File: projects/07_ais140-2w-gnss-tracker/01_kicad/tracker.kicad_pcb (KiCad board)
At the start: 4 copper layers, 60 x 45 mm, 174 parts, among them J1 VEHICLE 2x4, J2 BATTERY 18650, J3 USB-C, J4 DEBUG TC2050, J5 NANO-SIM, J6 LTE ANT, J7 GNSS ANT, Q1 BUK7M12-60EX, Q2 2N7002, Q3 MMBT3904, Q4 BUK9M53-60EX, SW1 RESET, SW2 BOOT, U1 LM74700-Q1, U10 W25Q128JV, U11 SIM7080G, U12 TXS0108E, U13 ESDA6V1-5SC6, U14 NEO-F10N, U15 IIM-42652, U16 RV-3028-C7, U2 LM5164-Q1, U3 BQ24074, U4 LC709203F, U5 TLV75733P, U6 TPS22917, U7 TPS22917, U8 ESP32-S3-WROOM-1-N8R2, U9 USBLC6-2SC6

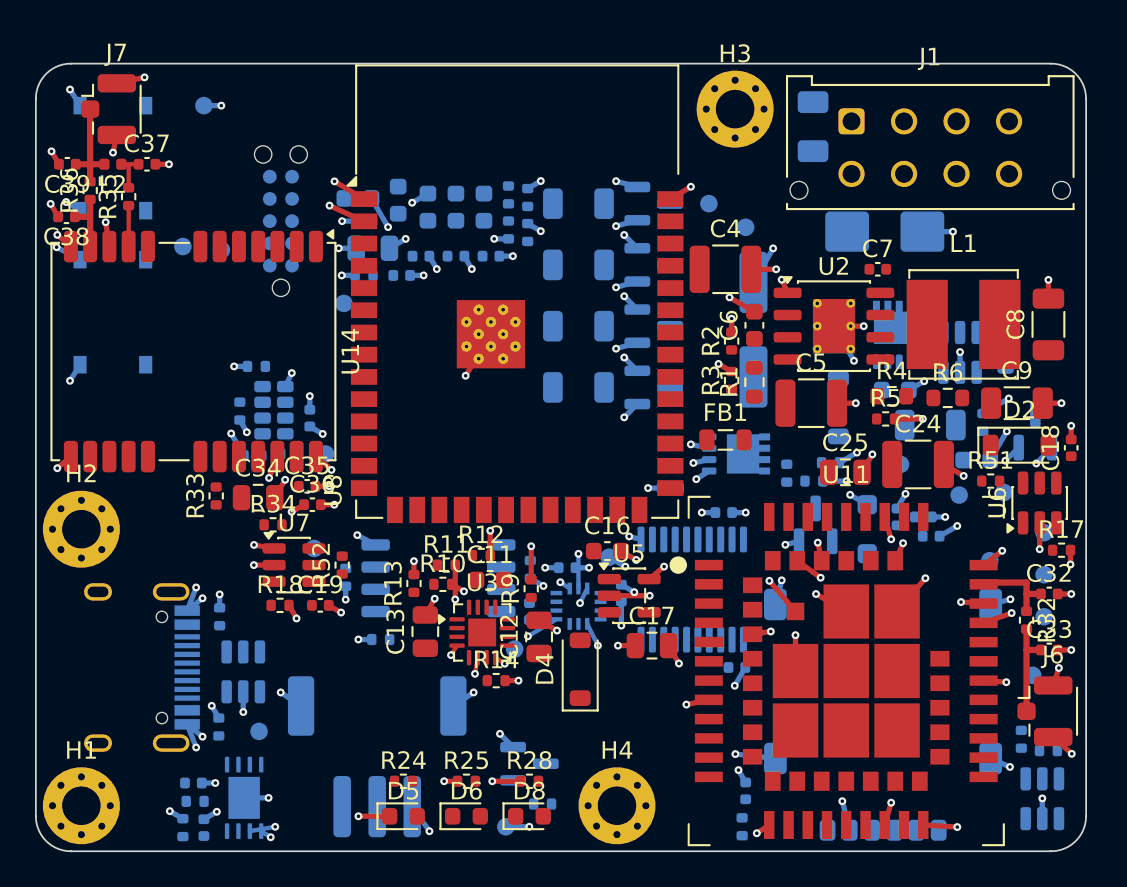
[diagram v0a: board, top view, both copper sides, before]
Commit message: Project 07: routed 4-layer PCB, fab outputs and 3D for the AIS-140 tracker
- 60x45 mm 4-layer board, double-sided assembly: KiCad DRC 0 errors / 0 unconnected,
  schematic parity clean, ERC clean
- Flow: anchors + greedy placer, GND/+3V3 fan-out, Freerouting 1.9, grid A* finisher
  with rip-up, RF via fences, edge/area stitching, island vias
- Gerbers + drill (zip), JLC BOM/CPL, engineering BOM, assembly PDFs, STEP + renders
  (envelope models for parts without a KiCad 3D model)
- Programming/JTAG via pogo test pads TP21-TP28 + native USB; R12 removed (TMR open)
- Design report updated with layout summary; DRC/ERC report added

Co-Authored-By: Claude Opus 5.5 <noreply@anthropic.com>
Claude-Session: https://claude.ai/code/session_01Hk6s8R6up8HYVQWXd3atVk
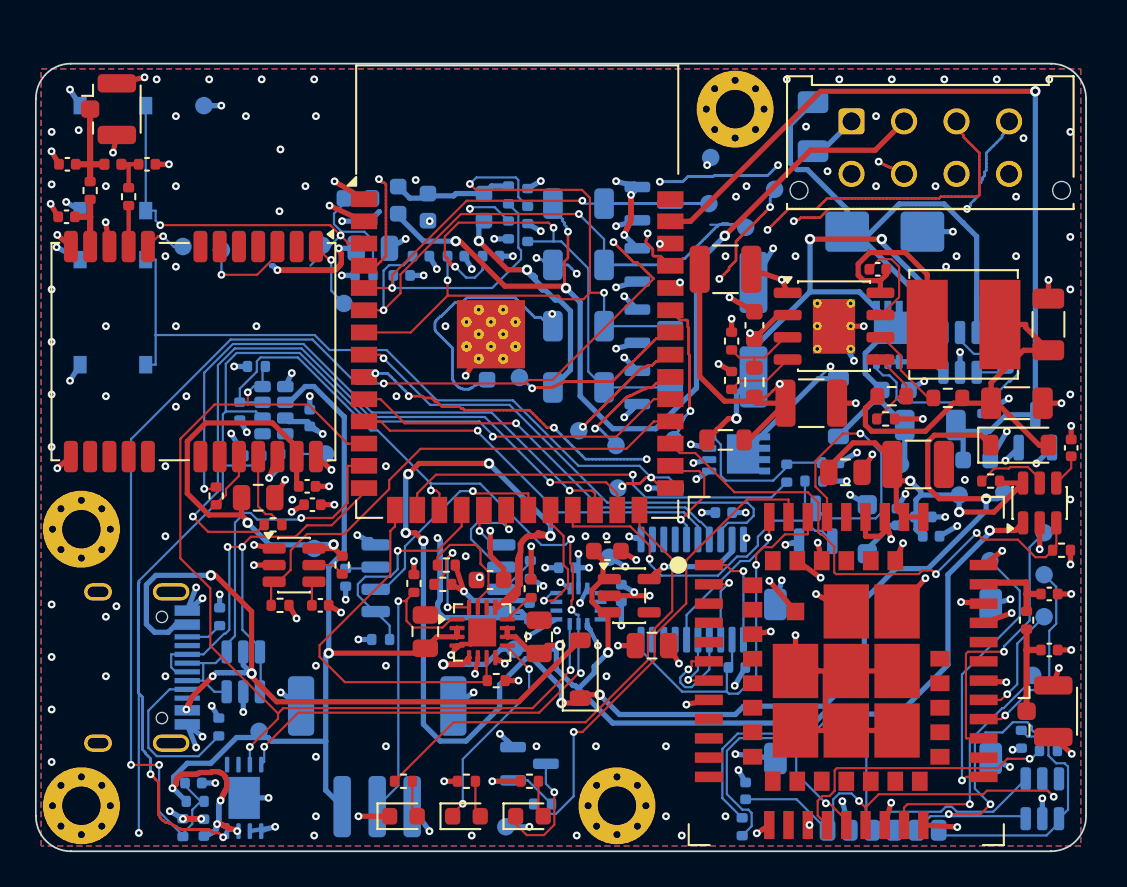
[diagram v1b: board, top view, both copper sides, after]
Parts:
- removed J4: DEBUG TC2050, Connector:Tag-Connect_TC2050-IDC-NL_2x05_P1.27mm_Vertical
- removed R12: 46.4k, Resistor_SMD:R_0402_1005Metric
- added TP21: JTAG_TMS, TestPoint:TestPoint_Pad_D1.0mm, B.Cu at (136.5, 121.5)
- added TP22: JTAG_TCK, TestPoint:TestPoint_Pad_D1.0mm, B.Cu at (133.1, 121.8)
- added TP23: JTAG_TDO, TestPoint:TestPoint_Pad_D1.0mm, B.Cu at (131.0, 121.0)
- added TP24: JTAG_TDI, TestPoint:TestPoint_Pad_D1.0mm, B.Cu at (127.6, 117.9)
- added TP25: U0TXD, TestPoint:TestPoint_Pad_D1.0mm, B.Cu at (138.6, 105.4)
- added TP26: U0RXD, TestPoint:TestPoint_Pad_D1.0mm, B.Cu at (142.2, 107.2)
- added TP27: ESP_EN, TestPoint:TestPoint_Pad_D1.0mm, B.Cu at (116.4, 110.4)
- added TP28: BOOT, TestPoint:TestPoint_Pad_D1.0mm, B.Cu at (133.2, 124.2)
- moved C47 9.26 mm to (125.8, 117.3)
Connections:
- U3 pad 14: CHG_TMR -> unconnected-(U3-TMR-Pad14)
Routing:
- net V5_IN: track 0.00 -> 100.3 mm, vias 0 -> 9
- net ALERT_N: track 0.00 -> 80.9 mm, vias 0 -> 4
- net VBAT_SENSE: track 0.00 -> 71.0 mm, vias 0 -> 5
- net VSYS: track 0.00 -> 60.5 mm, vias 0 -> 4
- net I2C_SCL: track 0.00 -> 57.5 mm, vias 0 -> 5
- net VBAT: track 0.00 -> 57.4 mm, vias 0 -> 5
- net I2C_SDA: track 0.00 -> 57.1 mm, vias 0 -> 3
- net IGN_RAW: track 0.00 -> 53.8 mm, vias 0 -> 4
- net VIN_SENSE: track 0.00 -> 49.1 mm, vias 0 -> 1
- net DIN1_RAW: track 0.00 -> 48.5 mm, vias 0 -> 3
- net VIN_PROT: track 0.00 -> 44.5 mm, vias 0 -> 3
- net BOOT: track 0.00 -> 44.2 mm, vias 0 -> 2
- net +3V3: track 32.7 -> 76.6 mm, vias 32 -> 35
- net VBUS: track 0.00 -> 42.9 mm, vias 0 -> 4
- net AIN1_RAW: track 0.00 -> 41.6 mm, vias 0 -> 5
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- added copper zone on B.Cu, net GND
- added copper zone on F.Cu, net GND
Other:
- board text added: "CRL-TRK-2W-01 A0"
